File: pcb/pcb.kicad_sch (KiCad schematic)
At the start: 47 parts, among them J1 USB_C_Receptacle_USB2.0_14P, J10 HC-05, J3 LCD, J5 M SEN, J7 DEBUG, J8 LCD CTRL, J9 USART3 TX, SW1 PWR SWITCH, U1 TLV62569DBV, U2 STM32F446RETx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

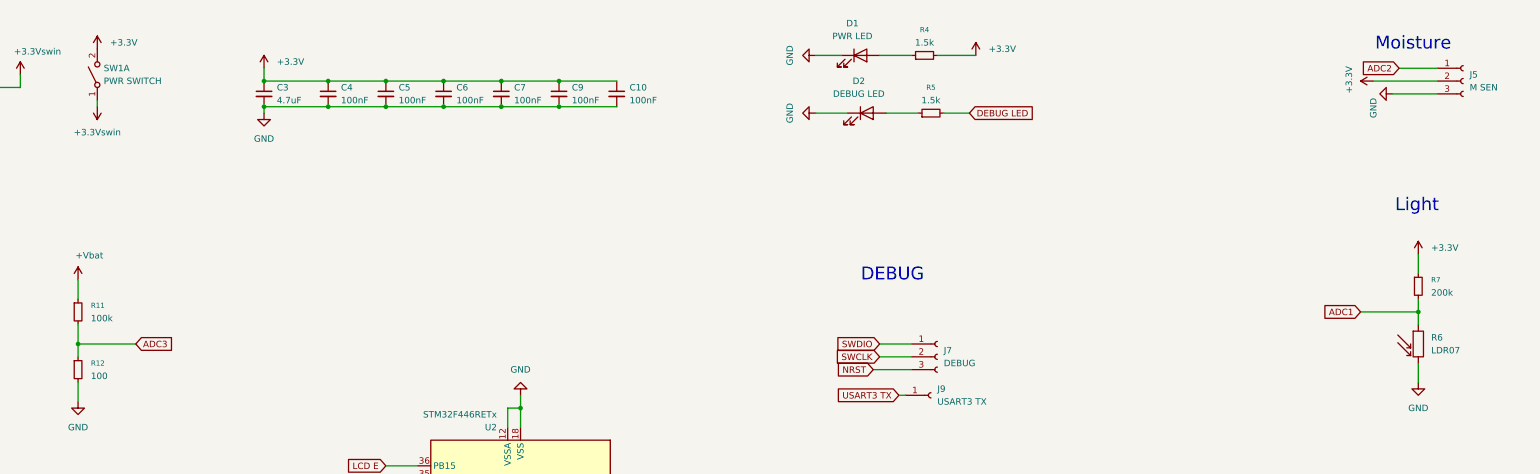
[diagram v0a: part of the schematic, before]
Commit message: Add battery sensor to pcb
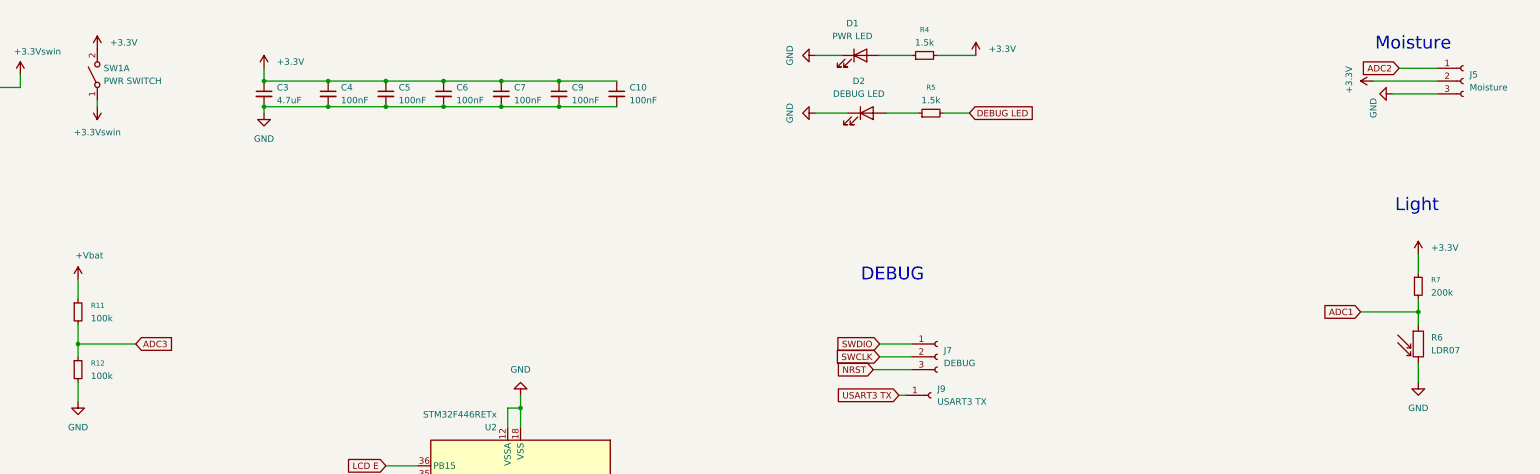
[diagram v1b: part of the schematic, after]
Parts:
- J5: value M SEN -> Moisture
- R11: footprint (none) -> Resistor_SMD:R_0603_1608Metric_Pad0.98x0.95mm_HandSolder
- R12: value 100 -> 100k; footprint (none) -> Resistor_SMD:R_0603_1608Metric_Pad0.98x0.95mm_HandSolder
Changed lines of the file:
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@@
 			)
 		)
-		(property "Value" "100"
+		(property "Value" "100k"
 			(at 113.03 91.4399 0)
 			(effects
@@
 			)
 		)
-		(property "Footprint" ""
+		(property "Footprint" "Resistor_SMD:R_0603_1608Metric_Pad0.98x0.95mm_HandSolder"
 			(at 110.49 90.17 0)
 			(effects
@@
 			)
 		)
-		(property "Value" "M SEN"
+		(property "Value" "Moisture"
 			(at 386.08 34.2899 0)
 			(effects
@@
 			)
 		)
-		(property "Footprint" ""
+		(property "Footprint" "Resistor_SMD:R_0603_1608Metric_Pad0.98x0.95mm_HandSolder"
 			(at 110.49 78.74 0)
 			(effects

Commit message: Add more vias and input capacitor to schematic
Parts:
- added C15: 10uF, Capacitor_SMD:C_0603_1608Metric_Pad1.08x0.95mm_HandSolder, symbol Device:C_Small
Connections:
- net +3.3V: now also C15.1
- net GND: now also C15.2
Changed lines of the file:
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@@
 	)
 	(junction
+		(at 67.31 240.03)
+		(diameter 0)
+		(color 0 0 0 0)
+	)
+	(junction
 		(at 57.15 156.21)
 		(diameter 0)
@@
 	(wire
 		(pts
+			(xy 67.31 242.57) (xy 67.31 240.03)
+		)
+		(stroke
+			(width 0)
+			(type default)
+		)
+	)
+	(wire
+		(pts
 			(xy 92.71 250.19) (xy 92.71 252.73)
 		)
@@
 	(wire
 		(pts
-			(xy 62.23 240.03) (xy 72.39 240.03)
+			(xy 62.23 240.03) (xy 67.31 240.03)
 		)
 		(stroke
@@
 	(wire
 		(pts
+			(xy 67.31 240.03) (xy 72.39 240.03)
+		)
+		(stroke
+			(width 0)
+			(type default)
+		)
+	)
+	(wire
+		(pts
 			(xy 52.07 96.52) (xy 58.42 96.52)
 		)
@@
 	)
 	(symbol
+		(lib_id "power:GND")
+		(at 67.31 247.65 0)
+		(unit 1)
+		(exclude_from_sim no)
+		(in_bom yes)
+		(on_board yes)
+		(dnp no)
+		(fields_autoplaced yes)
+		(property "Reference" "#PWR031"
+			(at 67.31 254 0)
+			(effects
+				(font
+					(size 1.27 1.27)
+				)
+				(hide yes)
+			)
+		)
+		(property "Value" "GND"
+			(at 67.31 252.73 0)
+			(effects
+				(font
+					(size 1.27 1.27)
+				)
+			)
+		)
+		(property "Footprint" ""
+			(at 67.31 247.65 0)
+			(effects
+				(font
+					(size 1.27 1.27)
+				)
+				(hide yes)
+			)
+		)
+		(property "Datasheet" ""
+			(at 67.31 247.65 0)
+			(effects
+				(font
+					(size 1.27 1.27)
+				)
+				(hide yes)
+			)
+		)
+		(property "Description" "Power symbol creates a global label with name \"GND\" , ground"
+			(at 67.31 247.65 0)
+			(effects
+				(font
+					(size 1.27 1.27)
+				)
+				(hide yes)
+			)
+		)
+		(pin "1"
+		)
+		(instances
+			(project ""
+				(path "/a02550bc-85b4-480d-868d-ccdfd0f6046d"
+					(reference "#PWR031")
+					(unit 1)
+				)
+			)
+		)
+	)
+	(symbol
 		(lib_id "Connector:USB_C_Receptacle_USB2.0_14P")
 		(at 36.83 111.76 0)
@@
 					(unit 1)
 				)
+			)
+		)
+	)
+	(symbol
+		(lib_id "Device:C_Small")
+		(at 67.31 245.11 0)
+		(unit 1)
+		(exclude_from_sim no)
+		(in_bom yes)
+		(on_board yes)
+		(dnp no)
+		(fields_autoplaced yes)
+		(property "Reference" "C15"
+			(at 69.85 243.8462 0)
+			(effects
+				(font
+					(size 1.27 1.27)
+				)
+				(justify left)
+			)
+		)
+		(property "Value" "10uF"
+			(at 69.85 246.3862 0)
+			(effects
+				(font
+					(size 1.27 1.27)
+				)
+				(justify left)
+			)
+		)
+		(property "Footprint" "Capacitor_SMD:C_0603_1608Metric_Pad1.08x0.95mm_HandSolder"
+			(at 67.31 245.11 0)
+			(effects
+				(font
+					(size 1.27 1.27)
+				)
+				(hide yes)
+			)
+		)
+		(property "Datasheet" "~"
+			(at 67.31 245.11 0)
+			(effects
+				(font
+					(size 1.27 1.27)
+				)
+				(hide yes)
+			)
+		)
+		(property "Description" "Unpolarized capacitor, small symbol"
+			(at 67.31 245.11 0)
+			(effects
+				(font
+					(size 1.27 1.27)
+				)
+				(hide yes)
+			)
+		)
+		(pin "2"
+		)
+		(pin "1"
+		)
+		(instances
+			(project "pcb"
+				(path "/a02550bc-85b4-480d-868d-ccdfd0f6046d"
+					(reference "C15")
+					(unit 1)
+				)

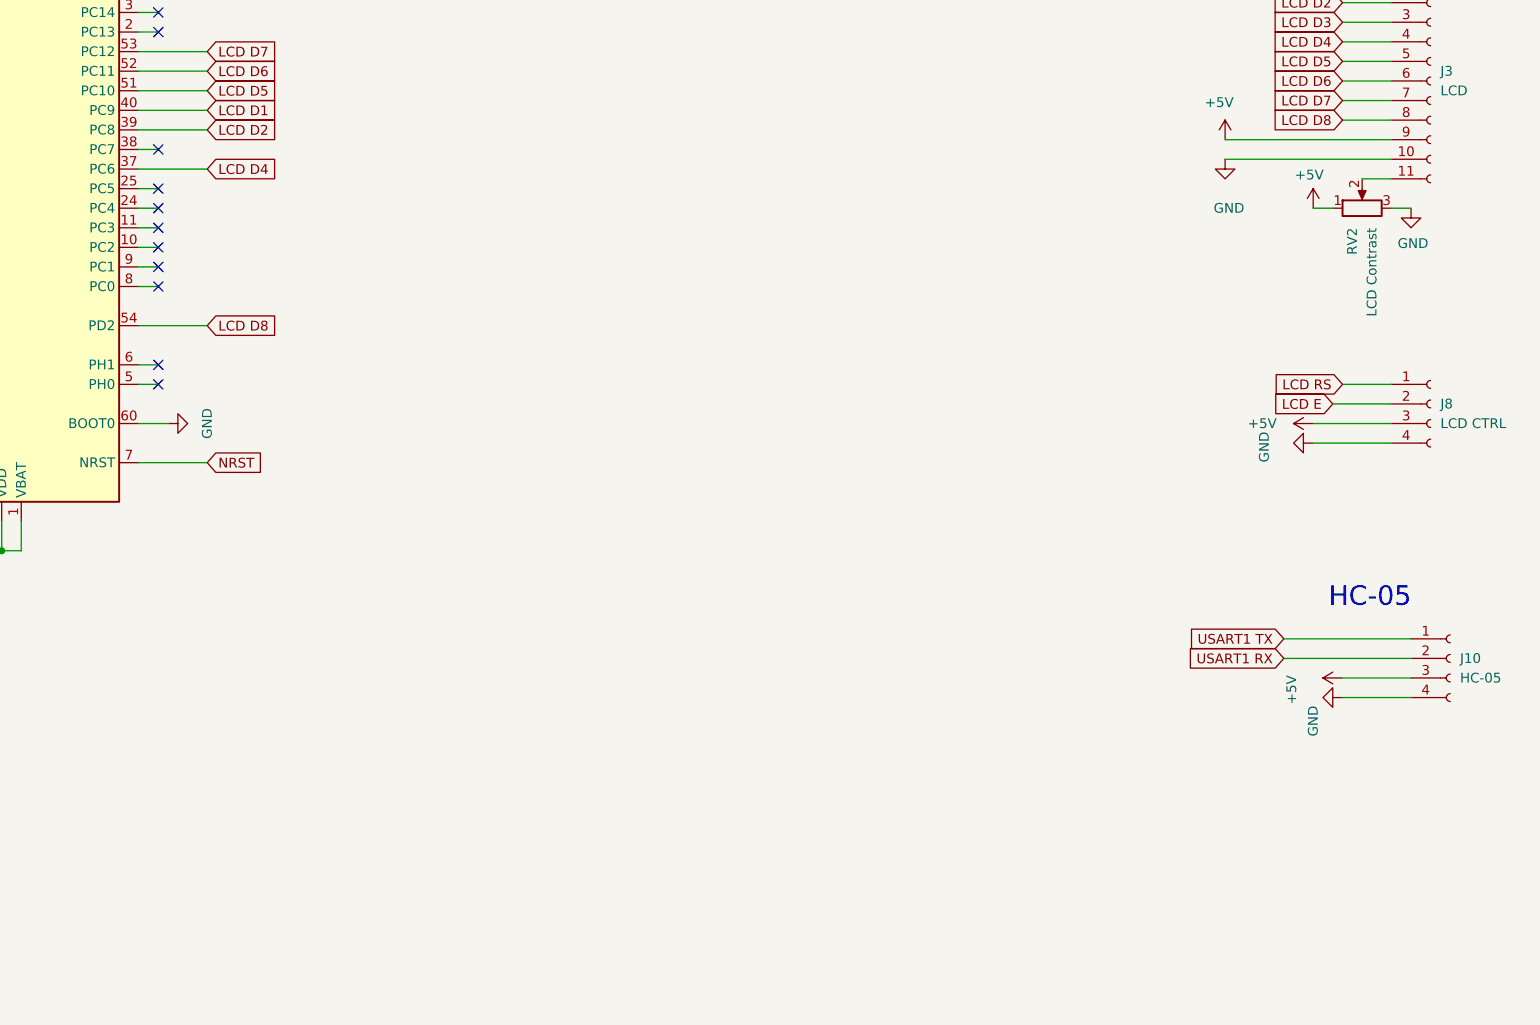
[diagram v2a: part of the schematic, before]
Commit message: Add volgo bluetooth module to pcb
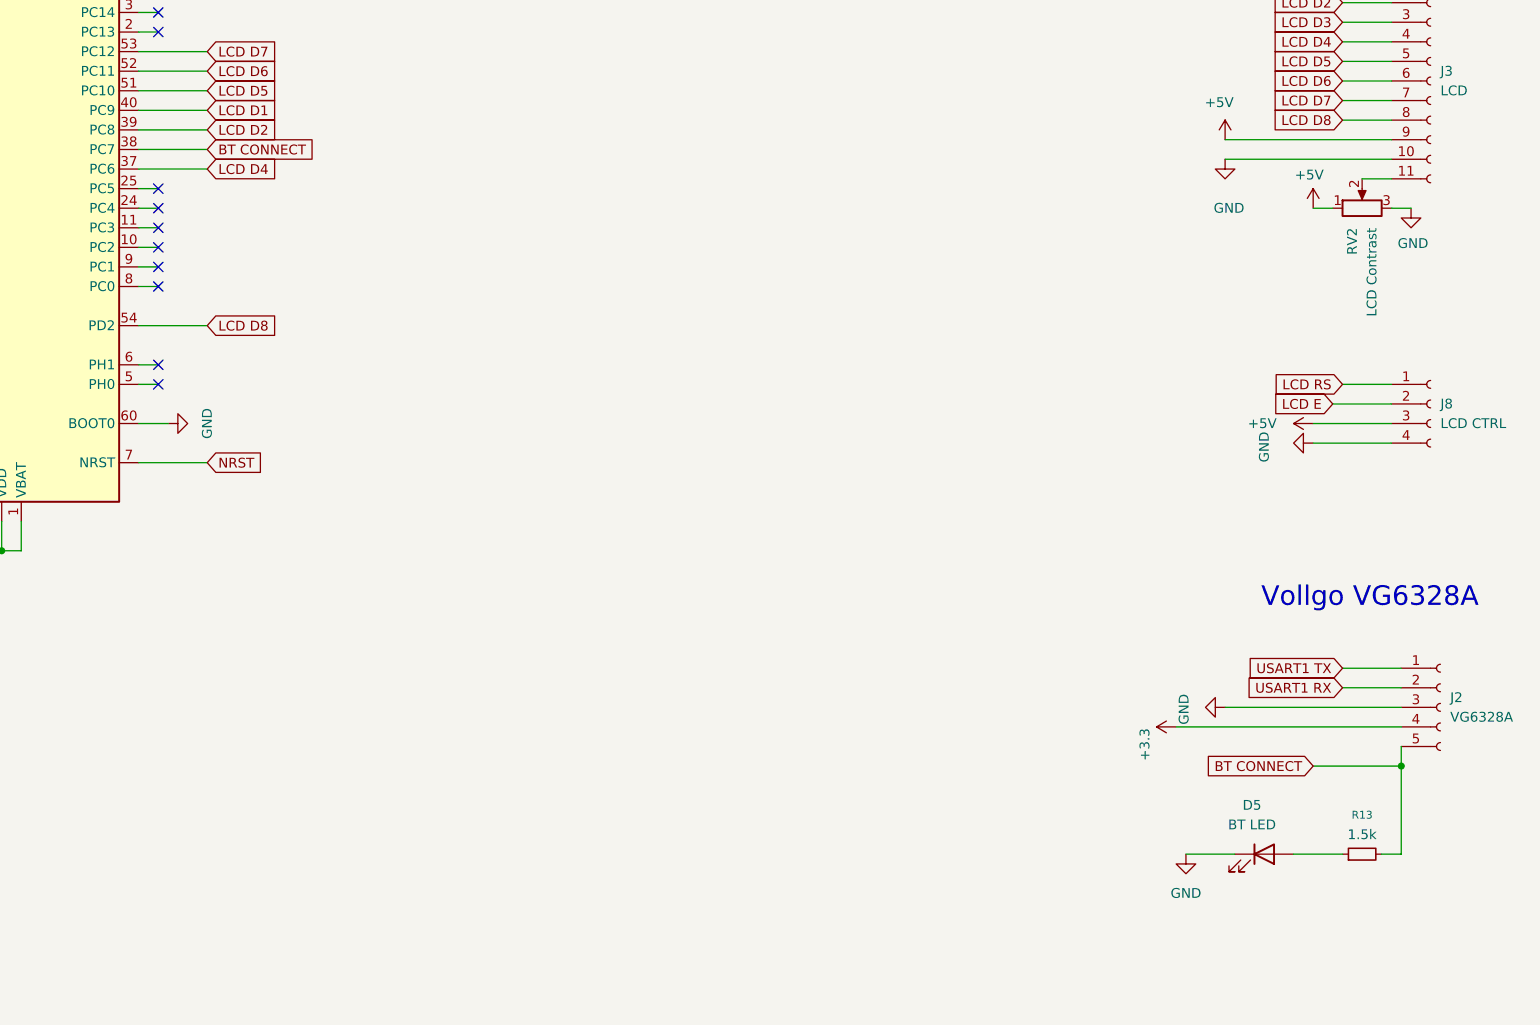
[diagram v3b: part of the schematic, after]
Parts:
- removed J10: HC-05, Connector_PinHeader_2.54mm:PinHeader_1x04_P2.54mm_Vertical, symbol Connector:Conn_01x04_Socket
- added D5: BT LED, LED_SMD:LED_0603_1608Metric_Pad1.05x0.95mm_HandSolder, symbol Device:LED
- added J2: VG6328A, custom:Vollgo VG6328A, symbol Connector:Conn_01x05_Socket
- added R13: 1.5k, Resistor_SMD:R_0603_1608Metric_Pad0.98x0.95mm_HandSolder, symbol Device:R_Small
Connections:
- net GND: now also D5.1 (K), J2.3 (Pin_3)
- net USART1 RX: now also J2.2 (Pin_2)
- net USART1 TX: now also J2.1 (Pin_1)
- net BT CONNECT: now reaches U2.38 (PC7)
- net BT CONNECT: now also J2.5 (Pin_5), R13.2
- new net: D5.2 (A), R13.1
- new net +3.3: J2.4 (Pin_4)
- no-connect marks 38 -> 37
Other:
- note added: "Vollgo VG6328A"
- note removed: "HC-05"

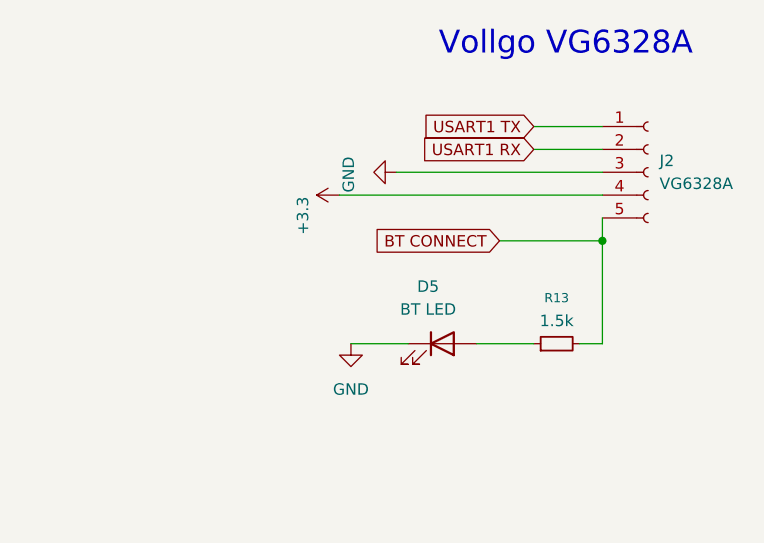
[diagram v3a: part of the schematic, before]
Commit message: Improve volgo bluetooth footprint and add pull up for bt connect pin
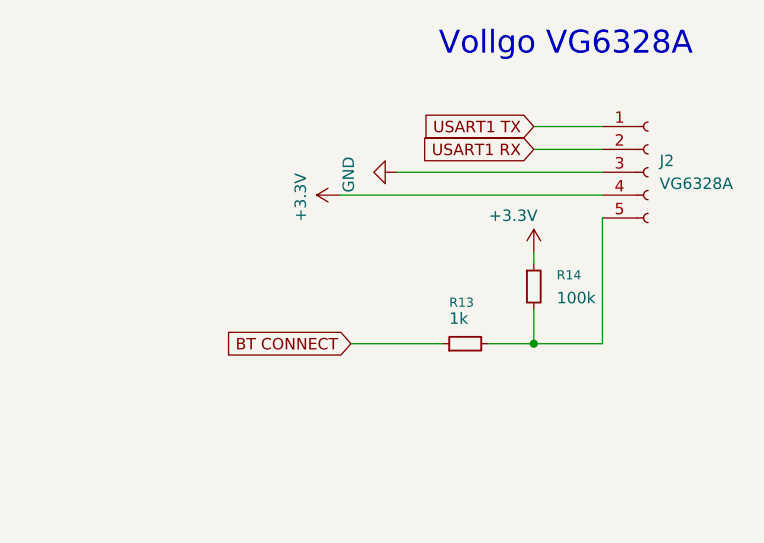
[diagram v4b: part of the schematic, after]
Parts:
- removed D5: BT LED, LED_SMD:LED_0603_1608Metric_Pad1.05x0.95mm_HandSolder, symbol Device:LED
- added R14: 100k, Resistor_SMD:R_0603_1608Metric_Pad0.98x0.95mm_HandSolder, symbol Device:R_Small
- R13: value 1.5k -> 1k
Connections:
- net +3.3 is gone; now on net +3.3V: J2.4 (Pin_4)
- net +3.3V: now also R14.1
- net BT CONNECT: now also R13.1; no longer J2.5 (Pin_5), R13.2
- new net: J2.5 (Pin_5), R13.2, R14.2

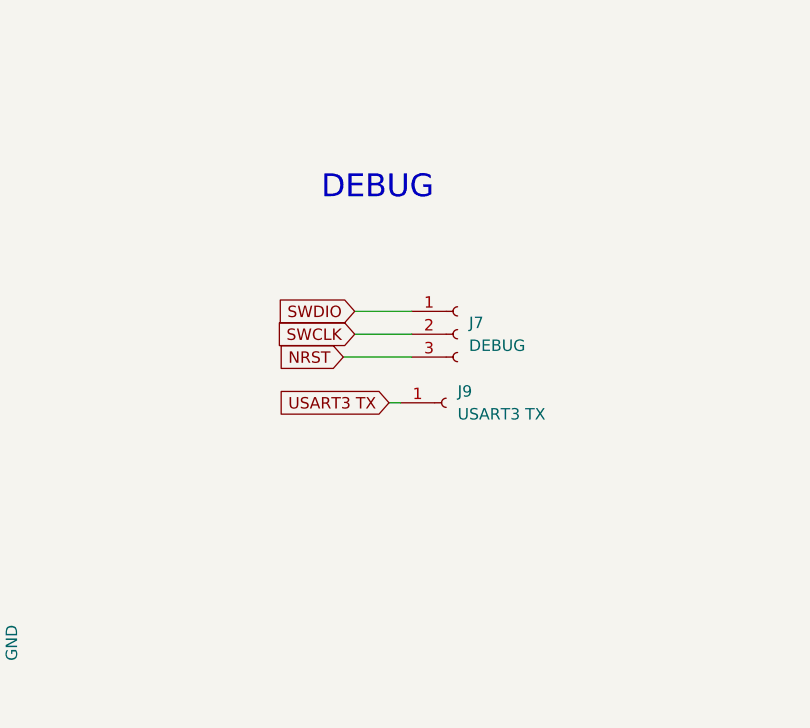
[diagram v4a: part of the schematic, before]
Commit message: add gnd sockets to debug headers
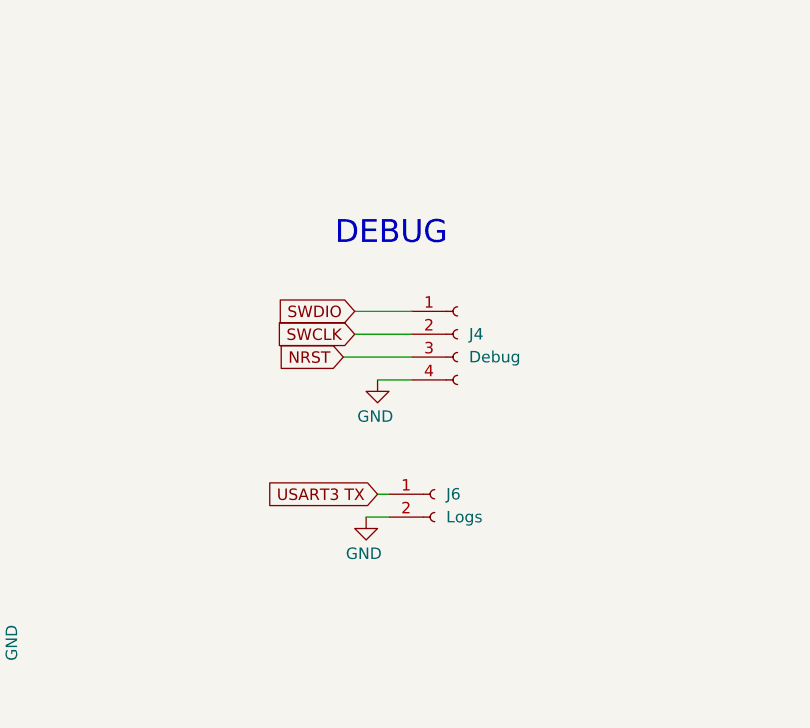
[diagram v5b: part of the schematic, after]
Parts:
- removed J7: DEBUG, Connector_PinHeader_2.54mm:PinHeader_1x03_P2.54mm_Vertical, symbol Connector:Conn_01x03_Socket
- removed J9: USART3 TX, Connector_PinSocket_2.54mm:PinSocket_1x01_P2.54mm_Vertical, symbol Connector:Conn_01x01_Socket
- added J4: Debug, Connector_PinHeader_2.54mm:PinHeader_1x04_P2.54mm_Vertical, symbol Connector:Conn_01x04_Socket
- added J6: Logs, Connector_PinHeader_2.54mm:PinHeader_1x02_P2.54mm_Vertical, symbol Connector:Conn_01x02_Socket
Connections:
- net GND: now also J4.4 (Pin_4), J6.2 (Pin_2)
- net NRST: now also J4.3 (Pin_3)
- net SWCLK: now also J4.2 (Pin_2)
- net SWDIO: now also J4.1 (Pin_1)
- net USART3 TX: now also J6.1 (Pin_1)

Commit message: tidy schematic
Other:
- note added: "Battery Monitor"
- note added: "Debug"
- note removed: "DEBUG"
- moved on the sheet: J2, J3, J4, J6, J8, R11, R12, R13, R14, R6, R7, RV2
